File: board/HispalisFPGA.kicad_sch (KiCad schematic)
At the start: 113 parts, among them SW1 SW_DIP_x08

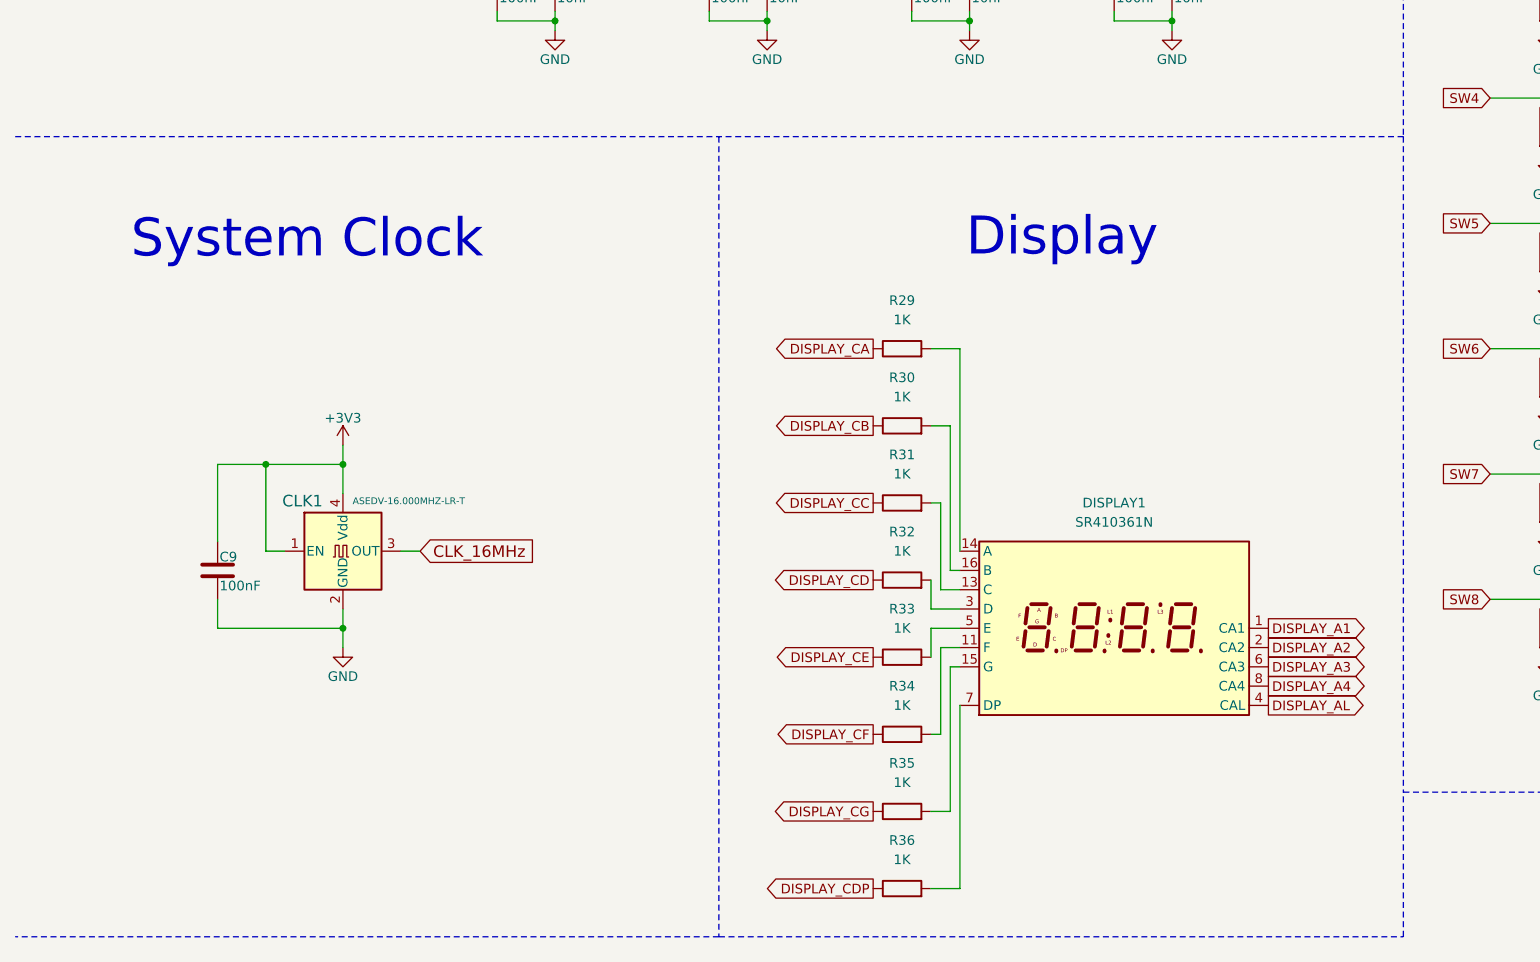
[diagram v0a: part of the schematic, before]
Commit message: Make all display pins activate on high signal from FPGA pins
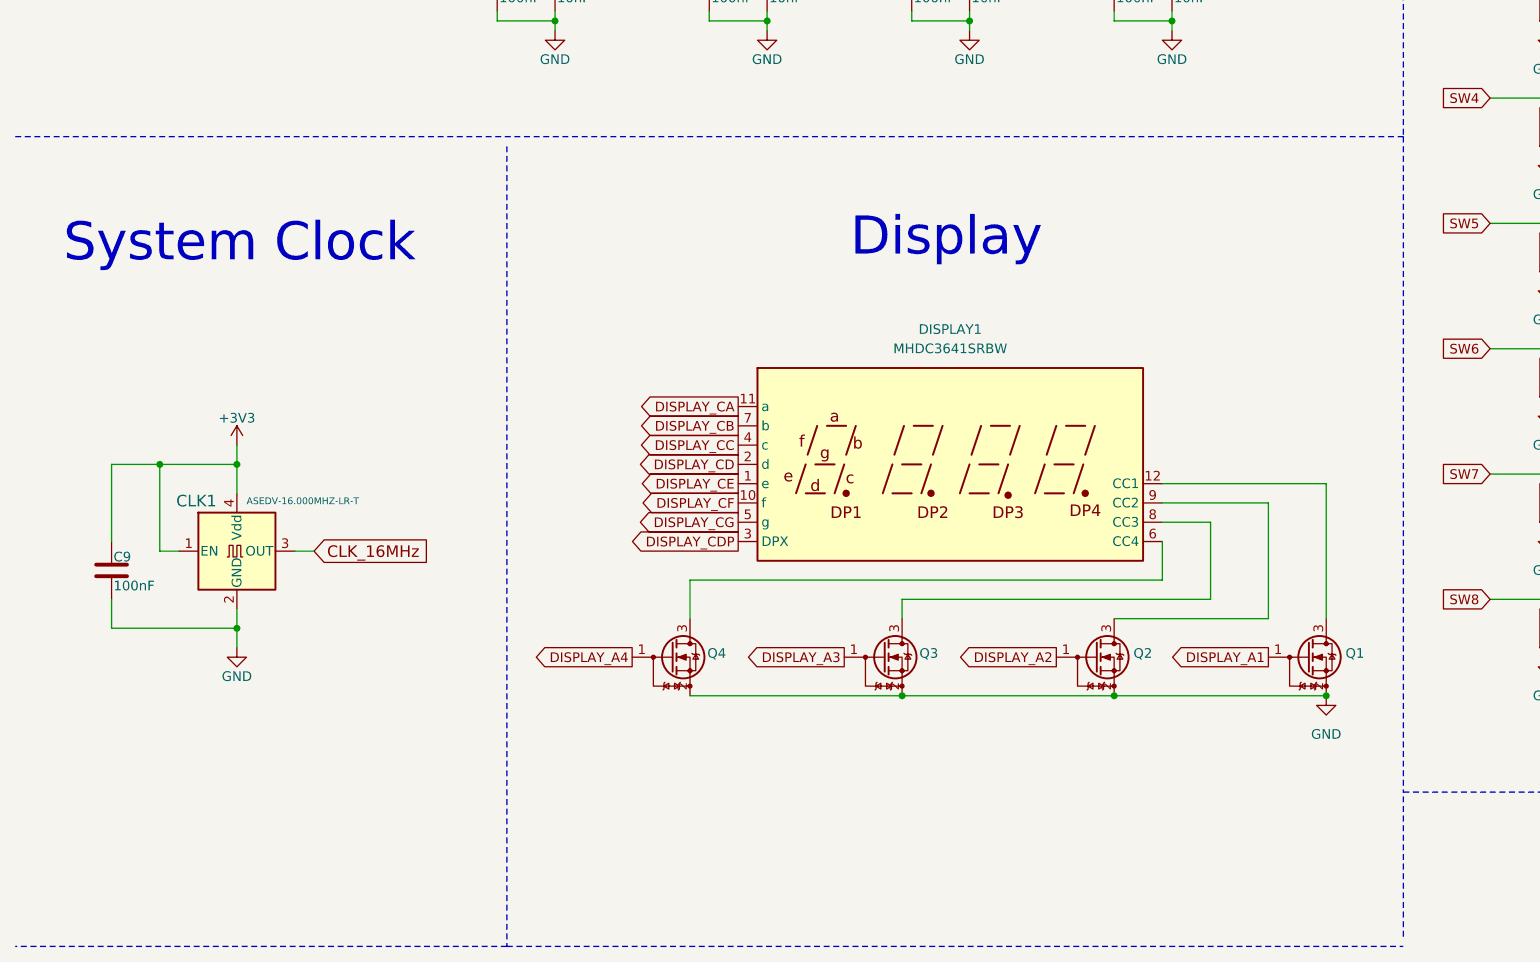
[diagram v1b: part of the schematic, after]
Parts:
- removed R29, R30, R31, R32, R33, R34, R35, R36: 1K, Resistor_SMD:R_0402_1005Metric, symbol Device:R
- added Q1, Q2, Q3, Q4: DMG1012T, Package_TO_SOT_SMD:SOT-523, symbol Transistor_FET:DMG1012T
- DISPLAY1: value SR410361N -> MHDC3641SRBW; footprint Display_7Segment:LTC-4627Jx -> Display_7Segment:CA56-12SRWA; symbol Display_Character:LTC-4627JR -> Display_Character:CC56-12SRWA; LCSC C132660 -> C3291494
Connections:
- net DISPLAY_AL is gone; now on net DISPLAY_CC: DISPLAY1.4 (c)
- net DISPLAY_A1: now also Q1.1 (G); no longer DISPLAY1.1 (CA1)
- net DISPLAY_A2: now also Q2.1 (G); no longer DISPLAY1.2 (CA2)
- net DISPLAY_A3: now also Q3.1 (G); no longer DISPLAY1.6 (CA3)
- net DISPLAY_A4: now also Q4.1 (G); no longer DISPLAY1.8 (CA4)
- net DISPLAY_CA: now also DISPLAY1.11 (a)
- net DISPLAY_CB: now also DISPLAY1.7 (b)
- net DISPLAY_CD: now also DISPLAY1.2 (d)
- net DISPLAY_CDP: now also DISPLAY1.3 (DPX)
- net DISPLAY_CE: now also DISPLAY1.1 (e)
- net DISPLAY_CF: now also DISPLAY1.10 (f)
- net DISPLAY_CG: now also DISPLAY1.5 (g)
- net GND: now also Q1.2 (S), Q2.2 (S), Q3.2 (S), Q4.2 (S)
- net at DISPLAY1.9 (CC2): now also Q2.3 (D)
- new net: DISPLAY1.12 (CC1), Q1.3 (D)
- new net: DISPLAY1.6 (CC4), Q4.3 (D)
- new net: DISPLAY1.8 (CC3), Q3.3 (D)
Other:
- moved on the sheet: C9, CLK1

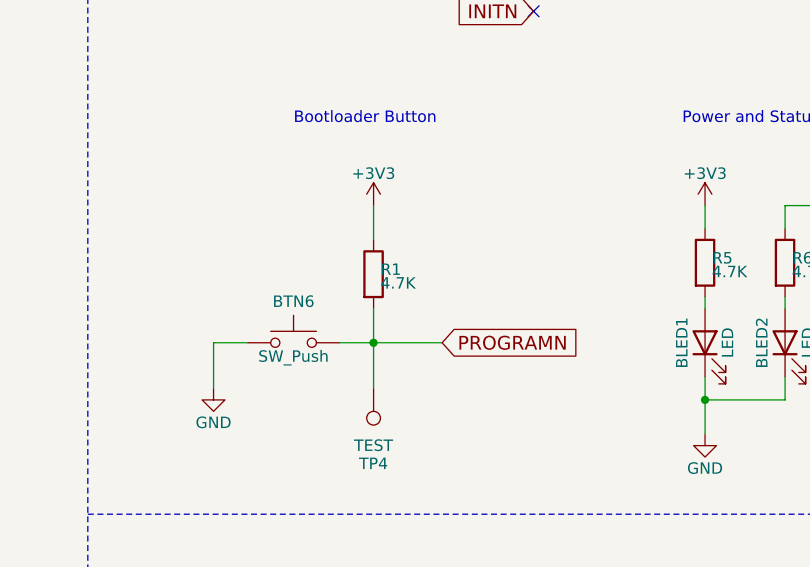
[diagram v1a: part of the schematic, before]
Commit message: Fix resistor value
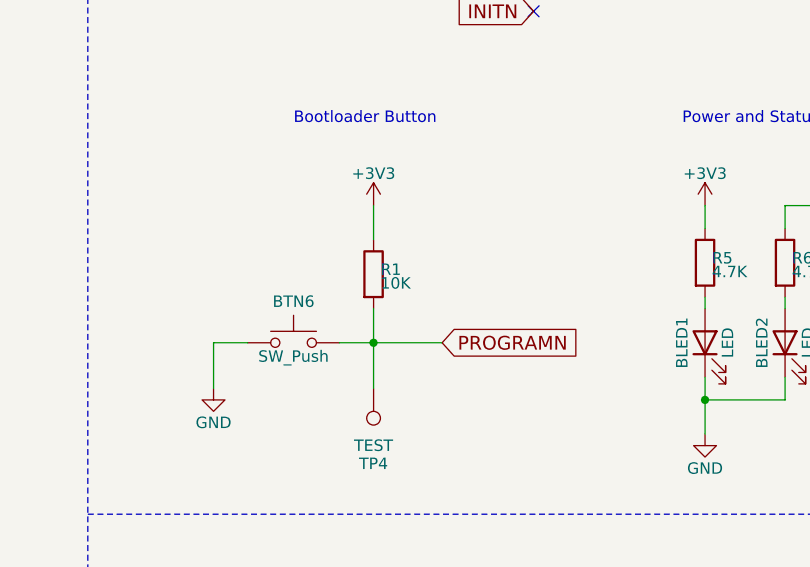
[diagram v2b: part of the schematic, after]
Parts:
- R1: value 4.7K -> 10K; LCSC C25900 -> C25744
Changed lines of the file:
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@@
 			)
 		)
-		(property "Value" "4.7K"
+		(property "Value" "10K"
 			(at 228.092 152.146 0)
 			(effects
@@
 			)
 		)
-		(property "LCSC" "C25900"
+		(property "LCSC" "C25744"
 			(at 227.33 151.13 0)
 			(effects

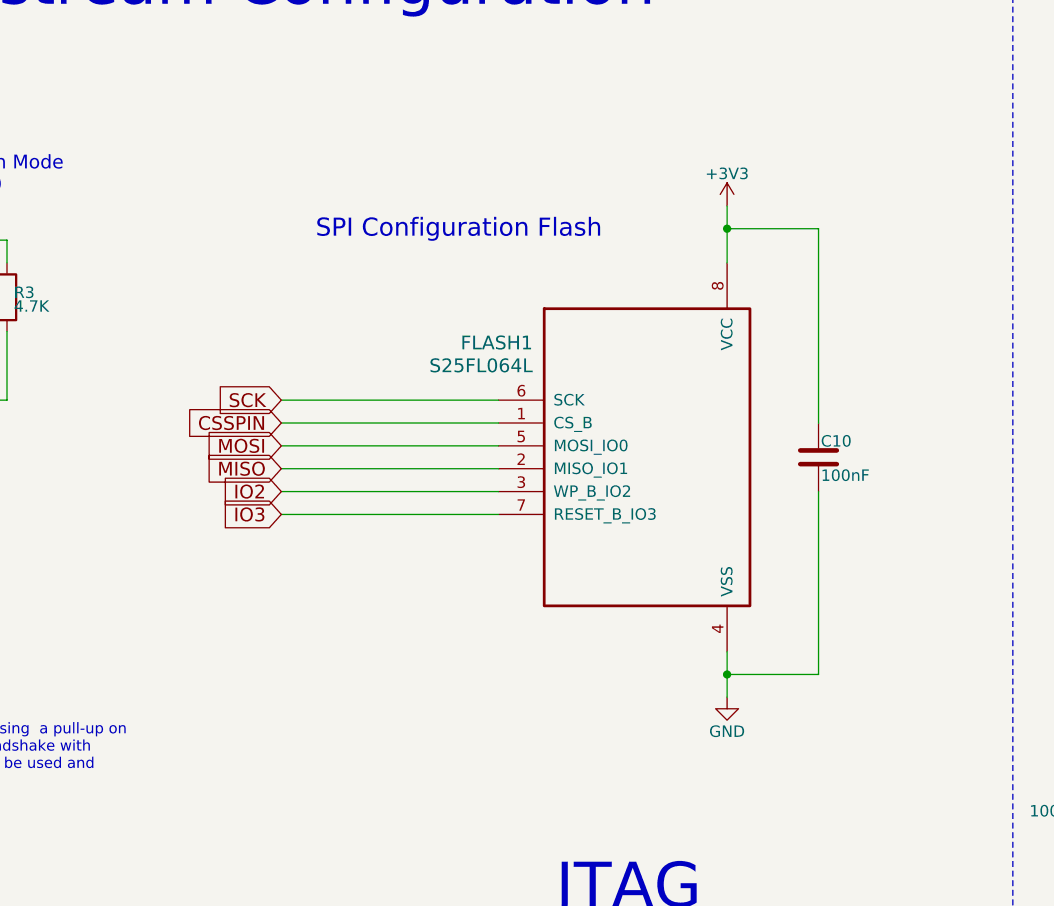
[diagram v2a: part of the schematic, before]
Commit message: Replace SPI flash device for a cheaper one
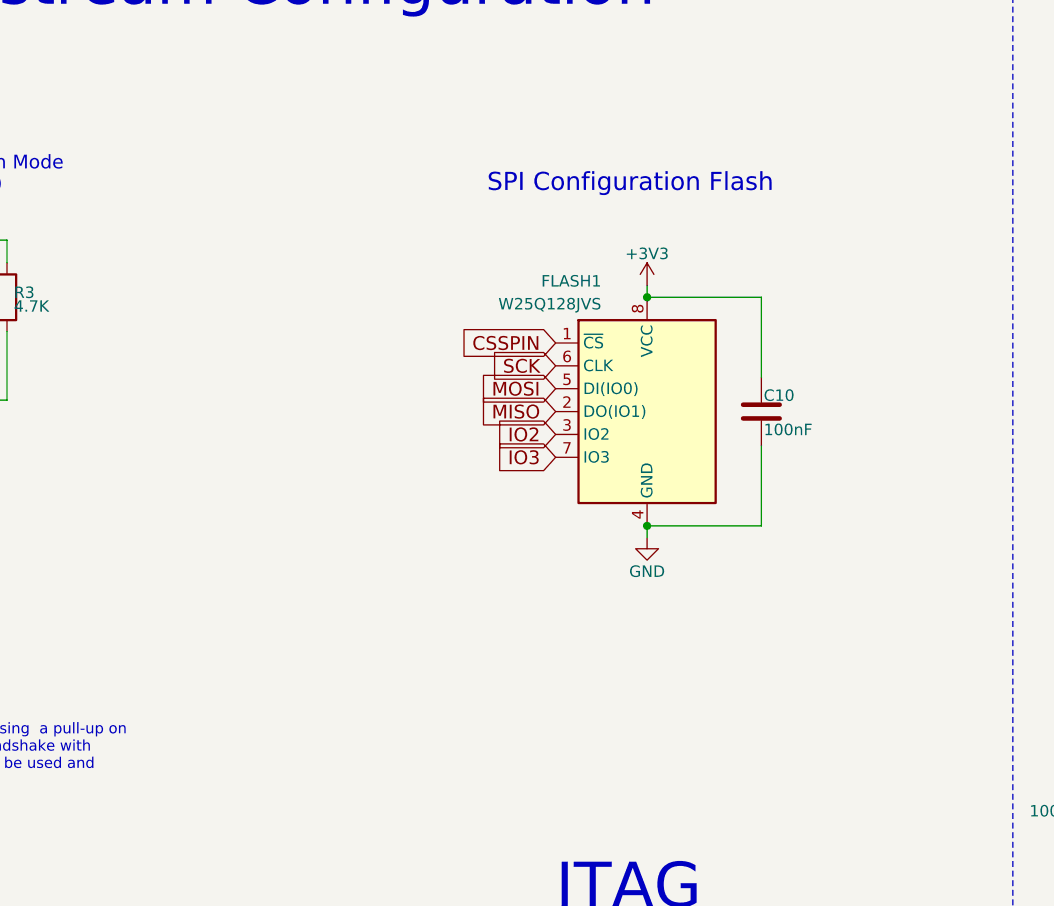
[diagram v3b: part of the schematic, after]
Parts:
- removed FLASH1: S25FL064L, Package_SO:SOIC-8_5.275x5.275mm_P1.27mm, symbol HispalisFPGA:S25FL064L-Components
- added FLASH1: W25Q128JVS, Package_SO:SOIC-8_5.23x5.23mm_P1.27mm, symbol Memory_Flash:W25Q128JVS
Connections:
- net +3V3: now also FLASH1.8 (VCC)
- net CSSPIN: now also FLASH1.1 (~{CS})
- net GND: now also FLASH1.4 (GND)
- net IO2: now also FLASH1.3 (IO2)
- net IO3: now also FLASH1.7 (IO3)
- net MISO: now also FLASH1.2 (DO(IO1))
- net MOSI: now also FLASH1.5 (DI(IO0))
- net SCK: now also FLASH1.6 (CLK)
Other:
- moved on the sheet: C10

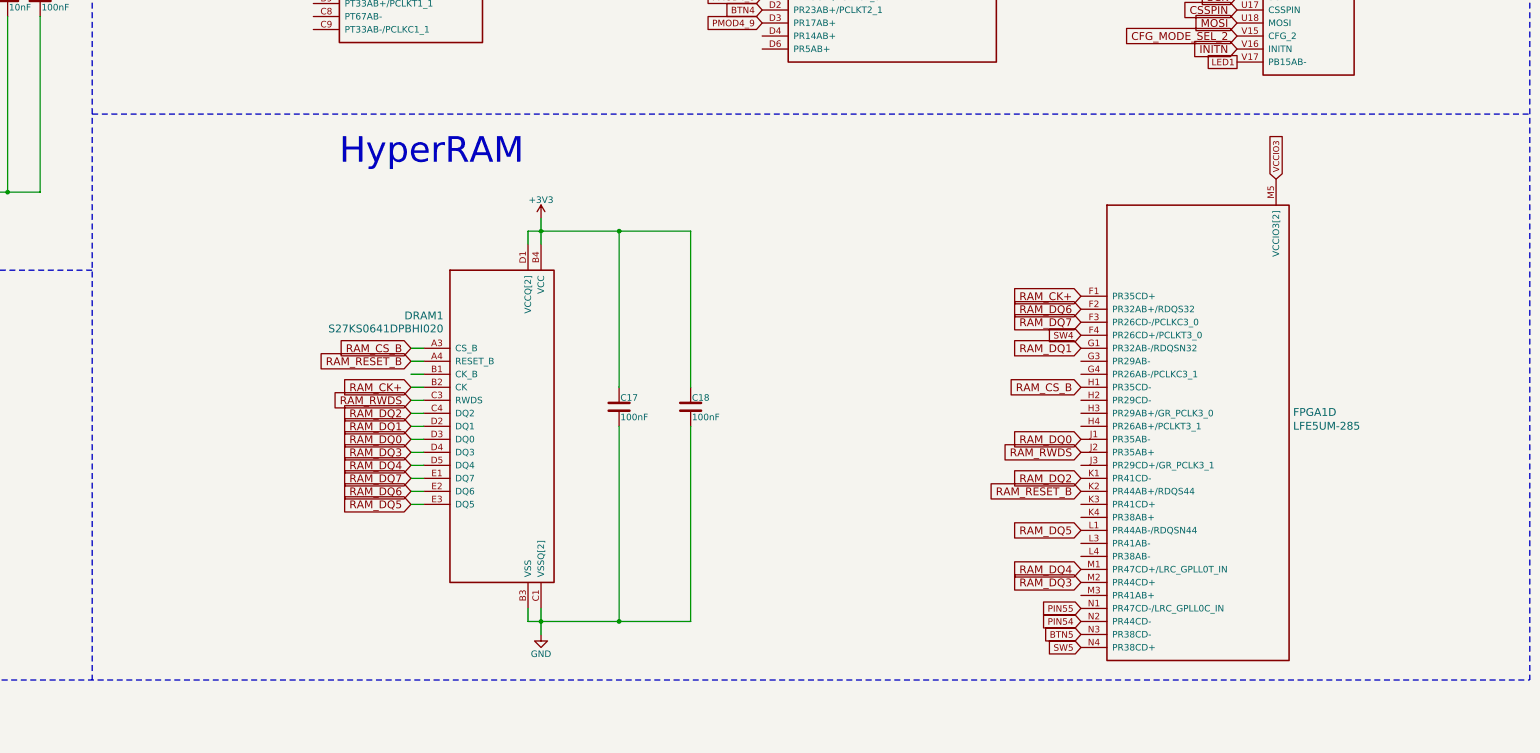
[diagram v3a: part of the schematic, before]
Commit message: Remove SDRAM block
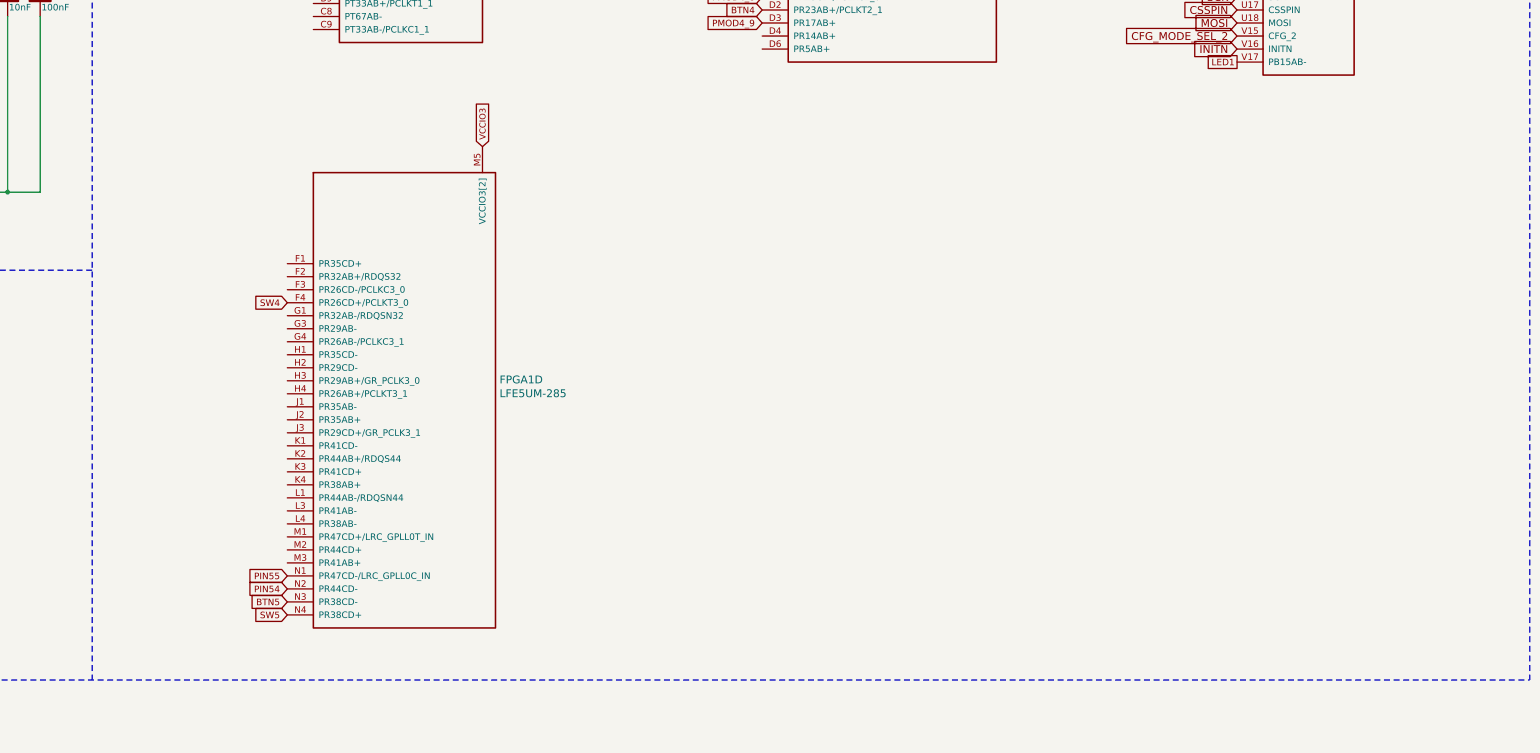
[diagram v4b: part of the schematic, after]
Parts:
- removed C17, C18: 100nF, Capacitor_SMD:C_0402_1005Metric, symbol Device:C
- removed DRAM1: S27KS0641DPBHI020, Footprints:FBGA-24, symbol HispalisFPGA:S27KS0641DPBHI020-Components
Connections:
- net RAM_CK+: no longer names the net of FPGA1.F1 (PR35CD+)
- net RAM_CS_B: no longer names the net of FPGA1.H1 (PR35CD-)
- net RAM_DQ0: no longer names the net of FPGA1.J1 (PR35AB-)
- net RAM_DQ1: no longer names the net of FPGA1.G1 (PR32AB-/RDQSN32)
- net RAM_DQ2: no longer names the net of FPGA1.K1 (PR41CD-)
- net RAM_DQ3: no longer names the net of FPGA1.M2 (PR44CD+)
- net RAM_DQ4: no longer names the net of FPGA1.M1 (PR47CD+/LRC_GPLL0T_IN)
- net RAM_DQ5: no longer names the net of FPGA1.L1 (PR44AB-/RDQSN44)
- net RAM_DQ6: no longer names the net of FPGA1.F2 (PR32AB+/RDQS32)
- net RAM_DQ7: no longer names the net of FPGA1.F3 (PR26CD-/PCLKC3_0)
- net RAM_RESET_B: no longer names the net of FPGA1.K2 (PR44AB+/RDQS44)
- net RAM_RWDS: no longer names the net of FPGA1.J2 (PR35AB+)
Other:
- note removed: "HyperRAM"
- moved on the sheet: FPGA1D

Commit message: Rearrange, cleanup and reannotate schematic
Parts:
- renumbered BTN6 to BTN1, BTN1 to BTN2, BTN2 to BTN3, BTN3 to BTN4, BTN4 to BTN5, BTN5 to BTN6, C9 to C1, C39 to C10, C2 to C11, C24 to C12, C21 to C13, C3 to C14, C22 to C15, C6 to C16, C40 to C17, C25 to C18, C34 to C19, C4 to C2, C7 to C20, C38 to C21, C26 to C22, C31 to C23, C8 to C24, C27 to C25, C32 to C26, C10 to C27, C42 to C28, C19 to C29, C23 to C3, C11 to C30, C13 to C31, C12 to C32, C14 to C33, C35 to C34, C36 to C35, C29 to C36, C15 to C37, C30 to C38, C41 to C39, C33 to C4, C16 to C40, C1 to C5, C37 to C6, C28 to C7, C20 to C8, C5 to C9, FB2 to FB1, FB1 to FB2, L2 to L1, L1 to L2, Q4 to Q1, Q3 to Q2, Q2 to Q3, Q1 to Q4, R37 to R1, R1 to R10, R2 to R11, R3 to R12, R5 to R13, R16 to R14, R17 to R15, R18 to R16, R19 to R17, R20 to R18, R6 to R19, R8 to R2, R4 to R20, R7 to R21, R9 to R3, R10 to R4, R11 to R5, R12 to R6, R13 to R7, R14 to R8, R15 to R9, TP4 to TP3
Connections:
- net PIN54: no longer names the net of FPGA1.N2 (PR44CD-)
- net PIN55: no longer names the net of FPGA1.N1 (PR47CD-/LRC_GPLL0C_IN)
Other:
- note added: "Board Connectors"
- note added: "FPGA IOs"
- note removed: "Board Connectors and FPGA IOs"
- moved on the sheet: FPGA1D, FPGA1E, FPGA1F, FPGA1G, JTAG1, PMOD1, PMOD2, PMOD3, PMOD4

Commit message: Replace 1.1V regulator
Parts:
- added C21: 100nF, Capacitor_SMD:C_0402_1005Metric, symbol Device:C
- added C26: 22uF, Capacitor_SMD:C_0603_1608Metric, symbol Device:C
- added C5: 10uF, Capacitor_SMD:C_0603_1608Metric, symbol Device:C
- added R2: 10K, Resistor_SMD:R_0402_1005Metric, symbol Device:R
- added R3: 12K, Resistor_SMD:R_0402_1005Metric, symbol Device:R
- 1V1_SW_REG1: value FAN53555UC04X -> TPS565208; footprint Footprints:WLCSP-20 -> Package_TO_SOT_SMD:SOT-23-6; symbol HispalisFPGA:FAN53555-Components -> Regulator_Switching:TPS565208
- C8: renamed from C7; value 10nF -> 100nF; LCSC C15195 -> C1525
- L2: value 330nH -> 2.2uH; footprint Inductor_SMD:L_1008_2520Metric -> Inductor_SMD:L_0805_2012Metric; JLC 1008 -> 0805; LCSC C375957 -> C2049745
- renumbered C9 to C10, C10 to C11, C11 to C12, C12 to C13, C13 to C14, C14 to C15, C15 to C16, C16 to C17, C17 to C18, C18 to C19, C19 to C20, C20 to C22, C21 to C23, C22 to C24, C23 to C25, C24 to C27, C25 to C28, C26 to C29, C27 to C30, C28 to C31, C29 to C32, C30 to C33, C31 to C34, C32 to C35, C33 to C36, C34 to C37, C35 to C38, C36 to C39, C37 to C40, C38 to C41, C39 to C42, C40 to C43, C5 to C6, C6 to C7, C8 to C9, R8 to R10, R9 to R11, R10 to R12, R11 to R13, R12 to R14, R13 to R15, R14 to R16, R15 to R17, R16 to R18, R17 to R19, R18 to R20, R19 to R21, R20 to R22, R21 to R23, R2 to R4, R3 to R5, R4 to R6, R5 to R7, R6 to R8, R7 to R9
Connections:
- net +5V: now also 1V1_SW_REG1.3 (VIN), 1V1_SW_REG1.5 (EN), C5.1; no longer 1V1_SW_REG1.A2 (EN), 1V1_SW_REG1.D1 (VIN[4]), 1V1_SW_REG1.D2 (VIN[4]), 1V1_SW_REG1.E1 (VIN[4]), 1V1_SW_REG1.E2 (VIN[4])
- net FPGA_PWR: now also C26.1, R2.1; no longer 1V1_SW_REG1.A4 (VOUT)
- net GND: now also 1V1_SW_REG1.1 (GND), C26.2, C5.2, R3.2; no longer 1V1_SW_REG1.A1 (VSEL), 1V1_SW_REG1.A3 (SCL), 1V1_SW_REG1.B1 (SDA), 1V1_SW_REG1.B2 (GND[6]), 1V1_SW_REG1.B3 (GND[6]), 1V1_SW_REG1.B4 (AGND), 1V1_SW_REG1.C1 (GND[6]), 1V1_SW_REG1.C2 (GND[6]), 1V1_SW_REG1.C3 (GND[6]), 1V1_SW_REG1.C4 (GND[6])
- new net: 1V1_SW_REG1.2 (SW), C21.2, L2.1
- new net: 1V1_SW_REG1.4 (VFB), R2.2, R3.1
- new net: 1V1_SW_REG1.6 (VBST), C21.1
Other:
- note added: "0.6V"
- note added: "1.1 Volt Switching Regulator"
- note added: "Following Ohm's and Kirchoff's laws: R22/R23 = (SW/VFB)-1"
- note removed: "0 = 1.1 V 1 = 1.2 V"
- note removed: "1.1/1.2 Volt Switching Regulator"
- moved on the sheet: C23, C4, C8, L2, TP1
